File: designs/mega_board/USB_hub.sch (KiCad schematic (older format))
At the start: 17 parts, among them U12 USB_HUB_FE1.1S, X2 YSX321SL 12MHz

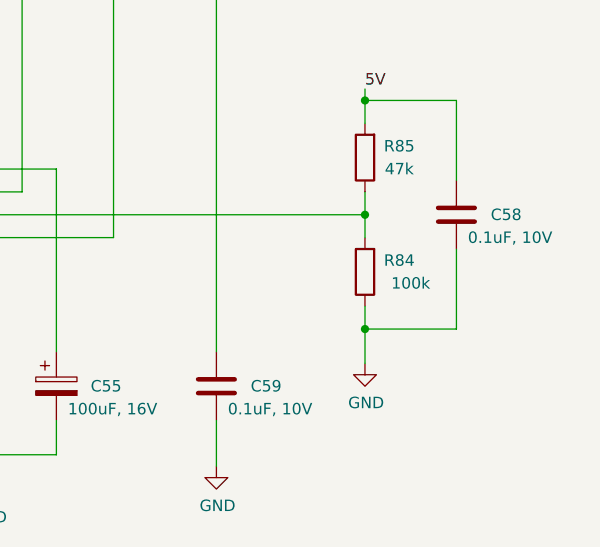
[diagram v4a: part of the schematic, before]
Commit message: Add BOM definition to all resistors
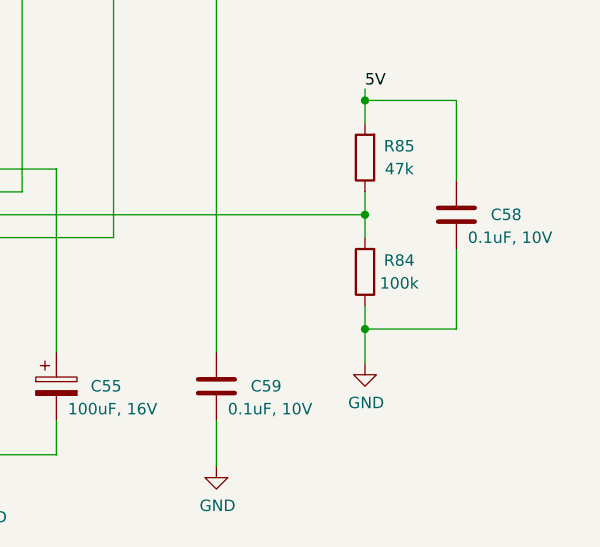
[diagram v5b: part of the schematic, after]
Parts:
- R81: Manufacturer (none) -> Panasonic Electronic Components; Manufacturer PN (none) -> ERJ-PA2F2701X; Supplier (none) -> DigiKey; Supplier PN (none) -> P124463DKR-ND
- R82, R83, R84, R86: Manufacturer (none) -> Panasonic Electronic Components; Manufacturer PN (none) -> ERJ-PA2F1003X; Supplier (none) -> DigiKey; Supplier PN (none) -> P17236DKR-ND
- R85: Manufacturer (none) -> Panasonic Electronic Components; Manufacturer PN (none) -> ERJ-PA2F4702X; Supplier (none) -> DigiKey; Supplier PN (none) -> P17234DKR-ND
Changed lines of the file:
@@
 F 2 "LibreRouter_MegaBoard:R0402" V 7580 2850 50  0001 C CNN
 F 3 "~" H 7650 2850 50  0001 C CNN
+F 4 "Panasonic Electronic Components" H 7650 2850 50  0001 C CNN "Manufacturer"
+F 5 "ERJ-PA2F1003X" H 7650 2850 50  0001 C CNN "Manufacturer PN"
+F 6 "DigiKey" H 7650 2850 50  0001 C CNN "Supplier"
+F 7 "P17236DKR-ND" H 7650 2850 50  0001 C CNN "Supplier PN"
 	1    7650 2850
 	-1   0    0    1
@@
 F 2 "LibreRouter_MegaBoard:R0402" V 7980 2850 50  0001 C CNN
 F 3 "~" H 8050 2850 50  0001 C CNN
+F 4 "Panasonic Electronic Components" H 8050 2850 50  0001 C CNN "Manufacturer"
+F 5 "ERJ-PA2F1003X" H 8050 2850 50  0001 C CNN "Manufacturer PN"
+F 6 "DigiKey" H 8050 2850 50  0001 C CNN "Supplier"
+F 7 "P17236DKR-ND" H 8050 2850 50  0001 C CNN "Supplier PN"
 	1    8050 2850
 	-1   0    0    1
@@
 F 2 "LibreRouter_MegaBoard:R0402" V 8380 2850 50  0001 C CNN
 F 3 "~" H 8450 2850 50  0001 C CNN
+F 4 "Panasonic Electronic Components" H 8450 2850 50  0001 C CNN "Manufacturer"
+F 5 "ERJ-PA2F1003X" H 8450 2850 50  0001 C CNN "Manufacturer PN"
+F 6 "DigiKey" H 8450 2850 50  0001 C CNN "Supplier"
+F 7 "P17236DKR-ND" H 8450 2850 50  0001 C CNN "Supplier PN"
 	1    8450 2850
 	-1   0    0    1
@@
 P 9550 4350
 F 0 "R84" H 9400 4300 50  0000 C CNN
-F 1 "100k" H 9350 4400 50  0000 C CNN
+F 1 "100k" H 9400 4400 50  0000 C CNN
 F 2 "LibreRouter_MegaBoard:R0402" V 9480 4350 50  0001 C CNN
 F 3 "~" H 9550 4350 50  0001 C CNN
+F 4 "Panasonic Electronic Components" H 9550 4350 50  0001 C CNN "Manufacturer"
+F 5 "ERJ-PA2F1003X" H 9550 4350 50  0001 C CNN "Manufacturer PN"
+F 6 "DigiKey" H 9550 4350 50  0001 C CNN "Supplier"
+F 7 "P17236DKR-ND" H 9550 4350 50  0001 C CNN "Supplier PN"
 	1    9550 4350
 	-1   0    0    1
@@
 F 2 "LibreRouter_MegaBoard:R0402" V 9480 3850 50  0001 C CNN
 F 3 "~" H 9550 3850 50  0001 C CNN
+F 4 "Panasonic Electronic Components" H 9550 3850 50  0001 C CNN "Manufacturer"
+F 5 "ERJ-PA2F4702X" H 9550 3850 50  0001 C CNN "Manufacturer PN"
+F 6 "DigiKey" H 9550 3850 50  0001 C CNN "Supplier"
+F 7 "P17234DKR-ND" H 9550 3850 50  0001 C CNN "Supplier PN"
 	1    9550 3850
 	-1   0    0    1
@@
 F 2 "LibreRouter_MegaBoard:R0402" V 5130 4800 50  0001 C CNN
 F 3 "~" H 5200 4800 50  0001 C CNN
+F 4 "Panasonic Electronic Components" H 5200 4800 50  0001 C CNN "Manufacturer"
+F 5 "ERJ-PA2F2701X" H 5200 4800 50  0001 C CNN "Manufacturer PN"
+F 6 "DigiKey" H 5200 4800 50  0001 C CNN "Supplier"
+F 7 "P124463DKR-ND" H 5200 4800 50  0001 C CNN "Supplier PN"
 	1    5200 4800
 	-1   0    0    1

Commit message: Add BOM definition for components. We need more iformation for all the components that are not defined.
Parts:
- X2: Manufacturer (none) -> ECS Inc.; Manufacturer PN (none) -> ECS-120-20-33-CKM-TR; Supplier (none) -> DigiKey; Supplier PN (none) -> XC1810DKR-ND
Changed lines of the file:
@@
 F 2 "LibreRouter_MegaBoard:SMARTPRJ_CRYSTAL-3.2-2.5" H 2600 3250 50  0001 C CNN
 F 3 "~" H 2600 3250 50  0001 C CNN
+F 4 "ECS Inc." H 2600 3250 50  0001 C CNN "Manufacturer"
+F 5 "ECS-120-20-33-CKM-TR" H 2600 3250 50  0001 C CNN "Manufacturer PN"
+F 6 "DigiKey" H 2600 3250 50  0001 C CNN "Supplier"
+F 7 "XC1810DKR-ND" H 2600 3250 50  0001 C CNN "Supplier PN"
 	1    2600 3250
 	0    -1   -1   0

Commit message: Add some missing BOM details for components that are not in common suppliers
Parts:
- U12: Manufacturer (none) -> Tangming; Manufacturer PN (none) -> FE1.1s
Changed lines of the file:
@@
 F 2 "LibreRouter_MegaBoard:USB_HUB_FE1.1S" H 5950 3750 50  0001 C CNN
 F 3 "" H 5950 3750 50  0001 C CNN
+F 4 "Tangming" H 5950 3750 50  0001 C CNN "Manufacturer"
+F 5 "FE1.1s" H 5950 3750 50  0001 C CNN "Manufacturer PN"
 	1    5950 3750
 	1    0    0    -1
